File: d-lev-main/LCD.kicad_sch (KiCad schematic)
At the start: 13 parts, among them Q4 BSS138

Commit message: more minor pusharounds and updates
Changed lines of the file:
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@@
     (effects (font (size 1.27 1.27)) (justify right bottom))
   )
-  (hierarchical_label "lcd{data[0..3],rs,e,pwm}" (shape input) (at 222.25 107.95 0) (fields_autoplaced)
+  (hierarchical_label "lcd{rs,e,pwm,data[0..3]}" (shape input) (at 222.25 107.95 0) (fields_autoplaced)
     (effects (font (size 1.27 1.27)) (justify left))
   )

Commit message: Pinned out FPGA and rearranged encoders again
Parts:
- R? (x4): footprint Resistor_SMD:R_0805_2012Metric_Pad1.20x1.40mm_HandSolder -> Resistor_SMD:R_0603_1608Metric
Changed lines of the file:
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@@
       (effects (font (size 1.27 1.27)))
     )
-    (property "Footprint" "Resistor_SMD:R_0805_2012Metric_Pad1.20x1.40mm_HandSolder" (at 72.39 113.03 0)
+    (property "Footprint" "Resistor_SMD:R_0603_1608Metric" (at 72.39 113.03 0)
       (effects (font (size 1.27 1.27)) hide)
     )
@@
       (effects (font (size 1.27 1.27)))
     )
-    (property "Footprint" "Resistor_SMD:R_0805_2012Metric_Pad1.20x1.40mm_HandSolder" (at 96.52 113.03 0)
+    (property "Footprint" "Resistor_SMD:R_0603_1608Metric" (at 96.52 113.03 0)
       (effects (font (size 1.27 1.27)) hide)
     )
@@
       (effects (font (size 1.27 1.27)) (justify right))
     )
-    (property "Footprint" "Resistor_SMD:R_0805_2012Metric_Pad1.20x1.40mm_HandSolder" (at 109.22 121.92 0)
+    (property "Footprint" "Resistor_SMD:R_0603_1608Metric" (at 109.22 121.92 0)
       (effects (font (size 1.27 1.27)) hide)
     )
@@
       (effects (font (size 1.27 1.27)) (justify right))
     )
-    (property "Footprint" "Resistor_SMD:R_0805_2012Metric_Pad1.20x1.40mm_HandSolder" (at 80.01 118.11 0)
-      (effects (font (size 1.27 1.27)) hide)
-    )
+    (property "Footprint" "Resistor_SMD:R_0603_1608Metric" (at 80.01 118.11 0)
+      (effects (font (size 1.27 1.27)) hide)
+    )

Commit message: mostly done routing
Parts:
- C21: footprint Capacitor_SMD:C_0805_2012Metric_Pad1.18x1.45mm_HandSolder -> Capacitor_SMD:C_0603_1608Metric
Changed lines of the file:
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@@
       (effects (font (size 1.27 1.27)) (justify left))
     )
-    (property "Footprint" "Capacitor_SMD:C_0805_2012Metric_Pad1.18x1.45mm_HandSolder" (at 87.63 118.11 0)
+    (property "Footprint" "Capacitor_SMD:C_0603_1608Metric" (at 87.63 118.11 0)
       (effects (font (size 1.27 1.27)) hide)
     )

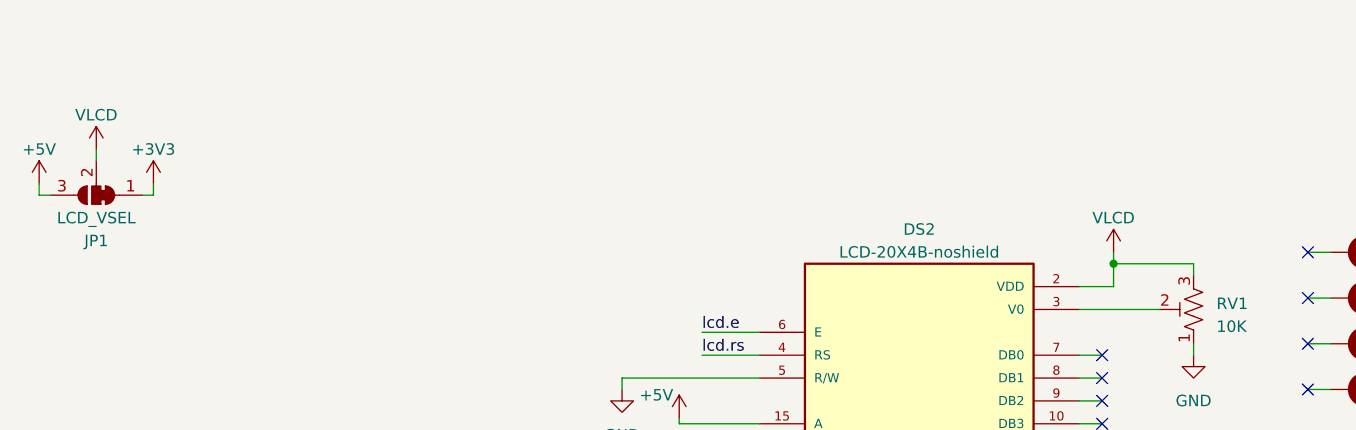
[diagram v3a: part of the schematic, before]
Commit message: four layer routes
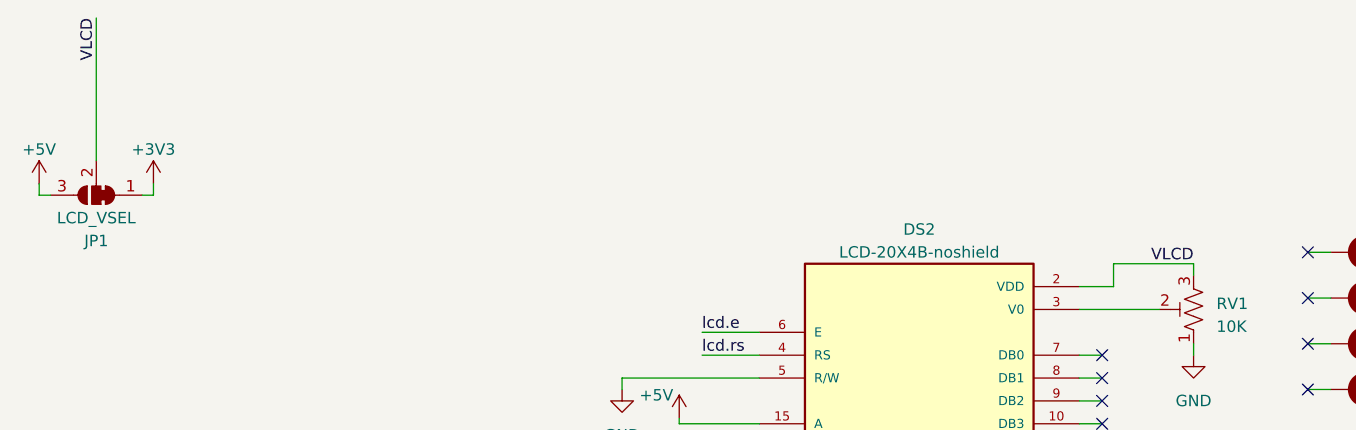
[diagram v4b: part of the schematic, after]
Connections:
- net +5V: no longer DS2.2 (VDD), JP1.2 (C), RV1.3
- new net VLCD: DS2.2 (VDD), JP1.2 (C), RV1.3
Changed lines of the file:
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@@
   (junction (at 87.63 113.03) (diameter 0) (color 0 0 0 0)
-  )
-  (junction (at 171.45 85.09) (diameter 0) (color 0 0 0 0)
   )
   (junction (at 83.82 125.73) (diameter 0) (color 0 0 0 0)
@@
     (stroke (width 0) (type default))
   )
-  (wire (pts (xy 58.42 72.39) (xy 58.42 73.66))
+  (wire (pts (xy 58.42 57.785) (xy 58.42 73.66))
     (stroke (width 0) (type default))
   )
@@
   )
   (wire (pts (xy 195.58 93.98) (xy 193.04 93.98))
-    (stroke (width 0) (type default))
-  )
-  (wire (pts (xy 171.45 83.82) (xy 171.45 85.09))
     (stroke (width 0) (type default))
   )
@@
     (effects (font (size 1.27 1.27)) (justify right bottom))
   )
+  (label "VLCD" (at 180.34 85.09 180) (fields_autoplaced)
+    (effects (font (size 1.27 1.27)) (justify right bottom))
+  )
   (label "lcd.rs" (at 125.73 95.25 0) (fields_autoplaced)
     (effects (font (size 1.27 1.27)) (justify left bottom))
@@
   )
   (label "lcd.data1" (at 180.34 107.95 180) (fields_autoplaced)
+    (effects (font (size 1.27 1.27)) (justify right bottom))
+  )
+  (label "VLCD" (at 58.42 57.785 270) (fields_autoplaced)
     (effects (font (size 1.27 1.27)) (justify right bottom))
   )
@@
         (path "/eb5e8bfd-9871-4528-bf57-58851bf63907/2925ec6e-2aba-4938-a246-f8cb5ac94723"
           (reference "H7") (unit 1)
-        )
-      )
-    )
-  )
-  (symbol (lib_id "power:+5V") (at 58.42 72.39 0) (unit 1)
-    (in_bom yes) (on_board yes) (dnp no) (fields_autoplaced)
-    (property "Reference" "#PWR045" (at 58.42 76.2 0)
-      (effects (font (size 1.27 1.27)) hide)
-    )
-    (property "Value" "VLCD" (at 58.42 68.58 0)
-      (effects (font (size 1.27 1.27)))
-    )
-    (property "Footprint" "" (at 58.42 72.39 0)
-      (effects (font (size 1.27 1.27)) hide)
-    )
-    (property "Datasheet" "" (at 58.42 72.39 0)
-      (effects (font (size 1.27 1.27)) hide)
-    )
-    (pin "1")
-    (instances
-      (project "dlev-mini"
-        (path "/eb5e8bfd-9871-4528-bf57-58851bf63907"
-          (reference "#PWR045") (unit 1)
-        )
-        (path "/eb5e8bfd-9871-4528-bf57-58851bf63907/2925ec6e-2aba-4938-a246-f8cb5ac94723"
-          (reference "#PWR045") (unit 1)
         )
       )
@@
         )
       )
-    )
-  )
-  (symbol (lib_id "power:+5V") (at 171.45 83.82 0) (unit 1)
-    (in_bom yes) (on_board yes) (dnp no) (fields_autoplaced)
-    (property "Reference" "#PWR042" (at 171.45 87.63 0)
-      (effects (font (size 1.27 1.27)) hide)
-    )
-    (property "Value" "VLCD" (at 171.45 80.01 0)
-      (effects (font (size 1.27 1.27)))
-    )
-    (property "Footprint" "" (at 171.45 83.82 0)
-      (effects (font (size 1.27 1.27)) hide)
-    )
-    (property "Datasheet" "" (at 171.45 83.82 0)
-      (effects (font (size 1.27 1.27)) hide)
-    )
-    (pin "1")
-    (instances
-      (project "dlev-mini"
-        (path "/eb5e8bfd-9871-4528-bf57-58851bf63907"
-          (reference "#PWR042") (unit 1)
-        )
-        (path "/eb5e8bfd-9871-4528-bf57-58851bf63907/2925ec6e-2aba-4938-a246-f8cb5ac94723"
-          (reference "#PWR041") (unit 1)
-        )
-      )

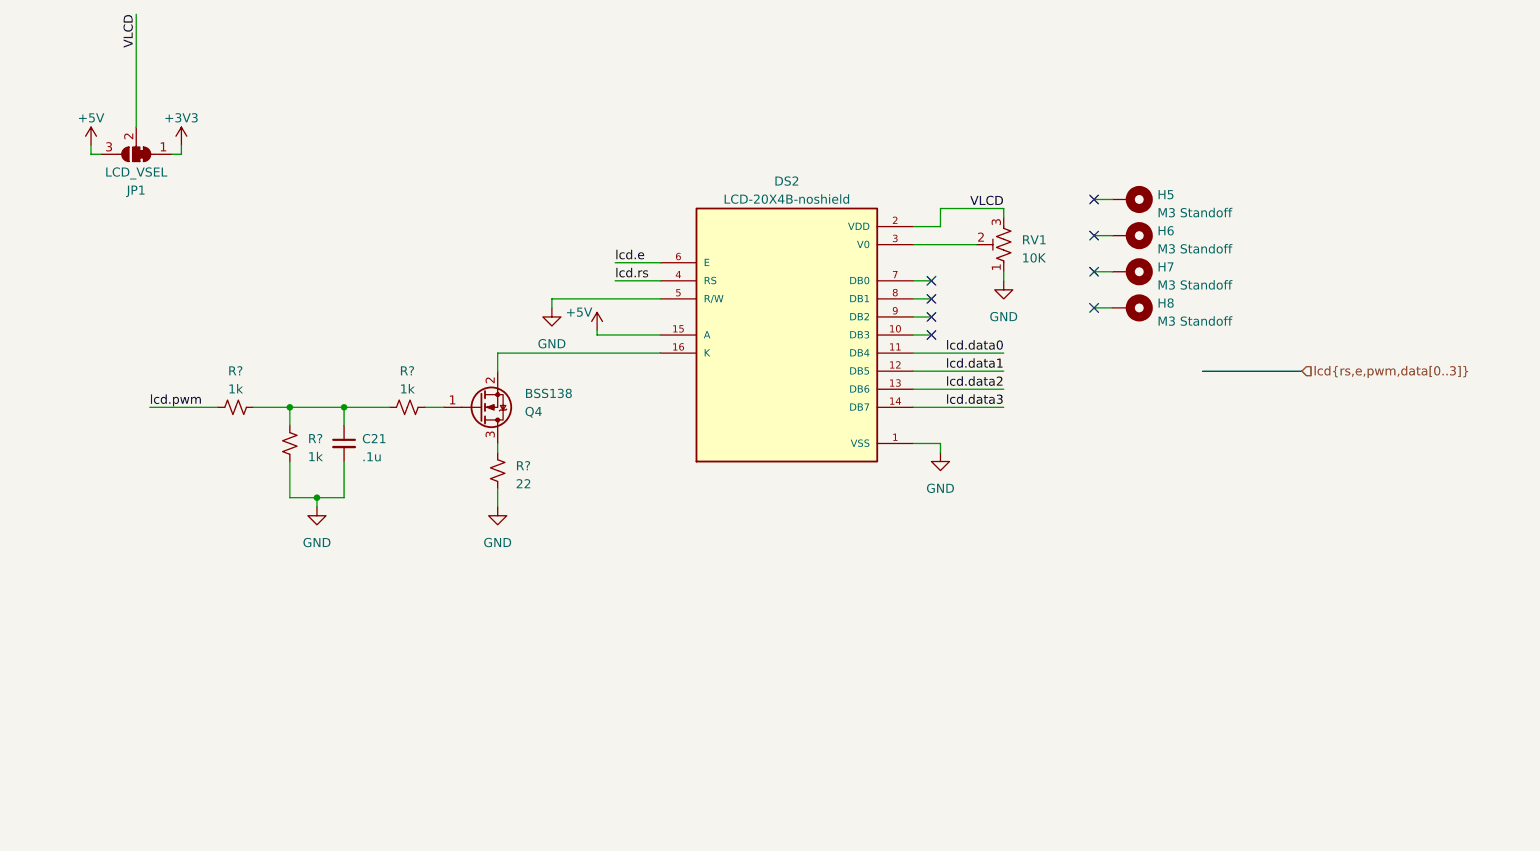
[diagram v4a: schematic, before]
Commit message: Via stitching around afe traces and add fix for lcd contrast pot
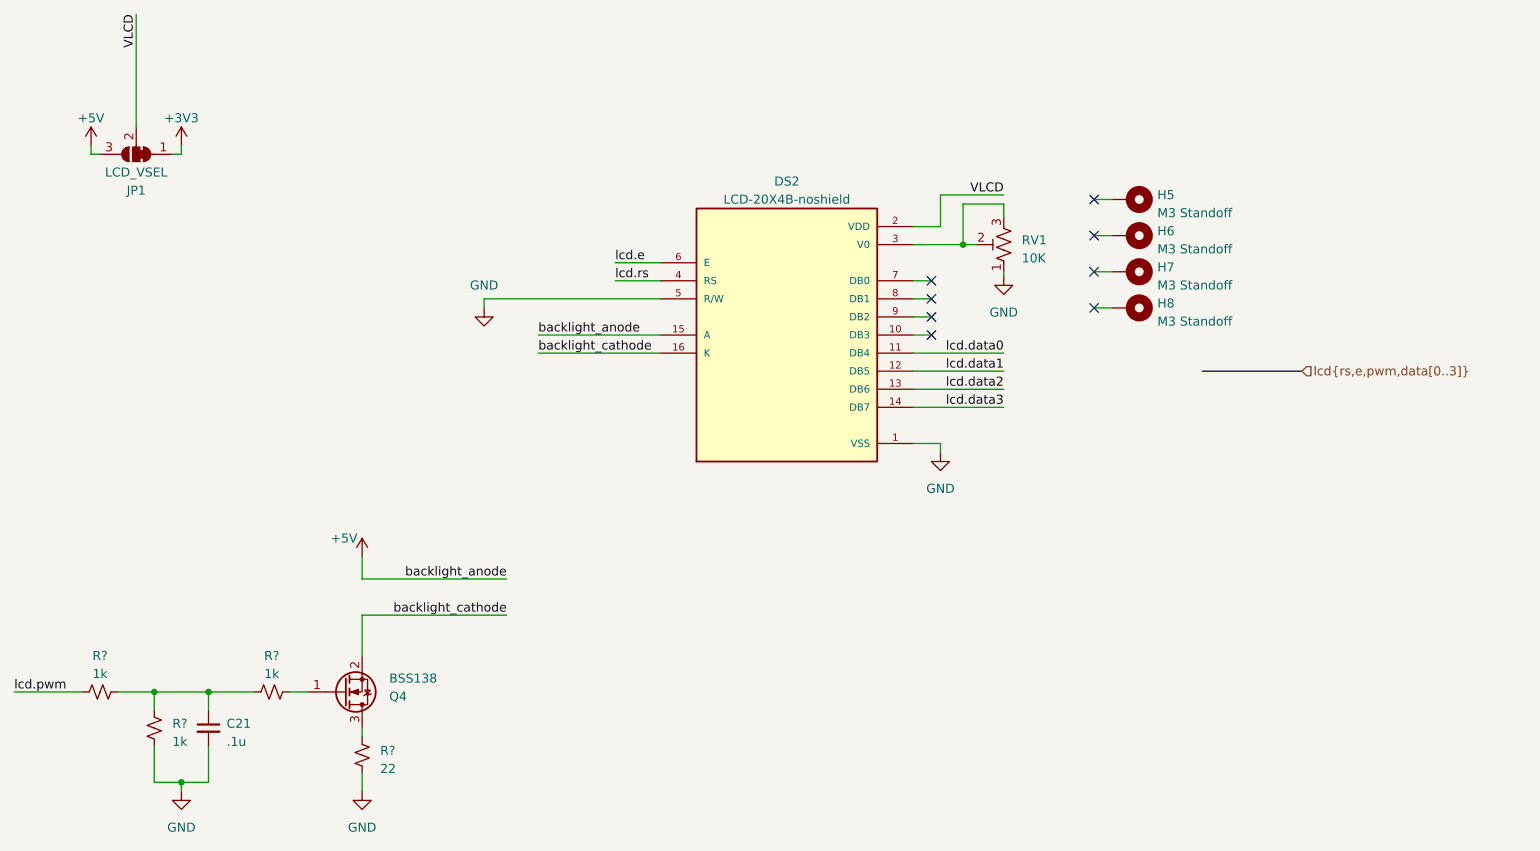
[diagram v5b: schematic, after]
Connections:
- net VLCD: no longer RV1.3
- net backlight_cathode: now reaches DS2.16 (K), Q4.2 (S)
- net at DS2.3 (V0), RV1.2: now also RV1.3
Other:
- moved on the sheet: C21, Q4, R?

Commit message: many many changes'
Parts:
- removed Q4: BSS138, Package_TO_SOT_SMD:SOT-23, symbol Transistor_FET:BSS138
- added Q2: MMBT3904, Package_TO_SOT_SMD:SOT-23, symbol Transistor_BJT:MMBT3904
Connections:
- net backlight_cathode: now also Q2.3 (C)
- net at R?.2: now also Q2.1 (B)
- net at R?.2: now also Q2.2 (E)
- net +5V renamed VDD
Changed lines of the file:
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@@
     )
   )
-  (symbol (lib_id "power:+5V") (at 90.17 133.985 0) (unit 1)
+  (symbol (lib_id "power:VDD") (at 90.17 133.985 0) (unit 1)
     (in_bom yes) (on_board yes) (dnp no)
     (property "Reference" "#PWR045" (at 90.17 137.795 0)
       (effects (font (size 1.27 1.27)) hide)
     )
-    (property "Value" "+5V" (at 87.63 131.445 0)
+    (property "Value" "VDD" (at 90.17 130.175 0)
       (effects (font (size 1.27 1.27)))
     )
@@
         )
         (path "/eb5e8bfd-9871-4528-bf57-58851bf63907/2925ec6e-2aba-4938-a246-f8cb5ac94723"
-          (reference "#PWR050") (unit 1)
+          (reference "#PWR0107") (unit 1)
         )
       )
@@
         (path "/eb5e8bfd-9871-4528-bf57-58851bf63907/2925ec6e-2aba-4938-a246-f8cb5ac94723"
           (reference "R6") (unit 1)
+        )
+      )
+    )
+  )
+  (symbol (lib_id "Transistor_BJT:MMBT3904") (at 87.63 153.035 0) (unit 1)
+    (in_bom yes) (on_board yes) (dnp no)
+    (property "Reference" "Q2" (at 93.345 152.4 0)
+      (effects (font (size 1.27 1.27)) (justify left))
+    )
+    (property "Value" "MMBT3904" (at 93.345 154.94 0)
+      (effects (font (size 1.27 1.27)) (justify left))
+    )
+    (property "Footprint" "Package_TO_SOT_SMD:SOT-23" (at 92.71 154.94 0)
+      (effects (font (size 1.27 1.27) italic) (justify left) hide)
+    )
+    (property "Datasheet" "https://www.onsemi.com/pub/Collateral/2N3903-D.PDF" (at 87.63 153.035 0)
+      (effects (font (size 1.27 1.27)) (justify left) hide)
+    )
+    (pin "1")
+    (pin "2")
+    (pin "3")
+    (instances
+      (project "dlev-mini"
+        (path "/eb5e8bfd-9871-4528-bf57-58851bf63907/2925ec6e-2aba-4938-a246-f8cb5ac94723"
+          (reference "Q2") (unit 1)
         )
       )
@@
     )
   )
-  (symbol (lib_id "power:+5V") (at 52.07 76.2 0) (unit 1)
+  (symbol (lib_id "power:VDD") (at 52.07 76.2 0) (unit 1)
     (in_bom yes) (on_board yes) (dnp no) (fields_autoplaced)
     (property "Reference" "#PWR046" (at 52.07 80.01 0)
       (effects (font (size 1.27 1.27)) hide)
     )
-    (property "Value" "+5V" (at 52.07 72.39 0)
+    (property "Value" "VDD" (at 52.07 72.39 0)
       (effects (font (size 1.27 1.27)))
     )
@@
         )
         (path "/eb5e8bfd-9871-4528-bf57-58851bf63907/2925ec6e-2aba-4938-a246-f8cb5ac94723"
-          (reference "#PWR044") (unit 1)
+          (reference "#PWR0106") (unit 1)
         )
       )
@@
         )
       )
-    )
-  )
-  (symbol (lib_id "Transistor_FET:BSS138") (at 87.63 153.035 0) (mirror x) (unit 1)
-    (in_bom yes) (on_board yes) (dnp no)
-    (property "Reference" "Q4" (at 93.98 153.67 0)
-      (effects (font (size 1.27 1.27)) (justify left))
-    )
-    (property "Value" "BSS138" (at 93.98 151.13 0)
-      (effects (font (size 1.27 1.27)) (justify left))
-    )
-    (property "Footprint" "Package_TO_SOT_SMD:SOT-23" (at 92.71 151.13 0)
-      (effects (font (size 1.27 1.27) italic) (justify left) hide)
-    )
-    (property "Datasheet" "https://www.onsemi.com/pub/Collateral/BSS138-D.PDF" (at 87.63 153.035 0)
-      (effects (font (size 1.27 1.27)) (justify left) hide)
-    )
-    (pin "1")
-    (pin "2")
-    (pin "3")
-    (instances
-      (project "dlev-mini"
-        (path "/eb5e8bfd-9871-4528-bf57-58851bf63907"
-          (reference "Q4") (unit 1)
-        )
-        (path "/eb5e8bfd-9871-4528-bf57-58851bf63907/2925ec6e-2aba-4938-a246-f8cb5ac94723"
-          (reference "Q1") (unit 1)
-        )
-      )
